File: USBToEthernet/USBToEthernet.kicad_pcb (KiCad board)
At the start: 2 copper layers, 61.3 x 30 mm, 54 parts, among them J1 0480372200, J2 L836-1J1T-43, SW1 SW_Push, U1 LAN7500-ABJZ, U2 NCP1117-3.3_SOT223, U3 93LCxxAxxOT, U4 USBLC6-2SC6, U6 AMS1117-1.2, Y1 25Mhz

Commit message: Reroute again
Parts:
- C1, C10, C11, C12, C13, C14, C15, C16, C17, C18, C19, C2, C20, C21, C26, C27, C3, C4, C5, C6, C7, C8, C9: footprint Capacitor_SMD:C_0603_1608Metric -> Capacitor_SMD:C_0402_1005Metric
- C22, C23, C24, C25: footprint Capacitor_SMD:C_0603_1608Metric -> Capacitor_SMD:C_0402_1005Metric; moved to F.Cu
- FB1, FB2, FB4: footprint Inductor_SMD:L_0603_1608Metric -> Inductor_SMD:L_0402_1005Metric
- FB3, FB5: footprint Inductor_SMD:L_0603_1608Metric -> Inductor_SMD:L_0402_1005Metric; moved to F.Cu
- R1, R10, R11, R12, R13, R2, R3, R4, R5, R6, R7, R8, R9: footprint Resistor_SMD:R_0603_1608Metric -> Resistor_SMD:R_0402_1005Metric
- moved FB1 19.0 mm to (79.3, 88.0)
- moved C6 18.7 mm to (84.9, 96.2), turned to -90 degrees
- moved C10 18.2 mm to (73.4, 93.5), turned to 180 degrees
- moved FB5 17.4 mm to (81.4, 81.3), turned to -90 degrees
- moved C13 17.3 mm to (72.0, 87.8)
- moved R3 17.1 mm to (100.4, 77.3)
- moved C11 17.1 mm to (76.7, 93.7), turned to 180 degrees
- moved C16 16.3 mm to (79.4, 89.1), turned to 180 degrees
- moved C25 16.2 mm to (80.9, 82.8)
- moved C17 15.8 mm to (79.3, 87.0), turned to 180 degrees
- moved C12 15.7 mm to (70.5, 88.2), turned to 180 degrees
- moved FB4 14.9 mm to (82.5, 81.4)
- moved J2 14.1 mm to (96.5, 88.7)
- moved C5 13.9 mm to (84.8, 94.2), turned to 90 degrees
- moved R4 13.8 mm to (102.3, 100.2)
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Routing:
- net GND: track 83.6 -> 30.5 mm, vias 42 -> 43
- net +1V2: track 134.6 -> 86.7 mm, vias 6 -> 9
- net /TR0: track 72.0 -> 46.3 mm, vias 6 -> 8
- net +3V3: track 176.4 -> 160.0 mm, vias 13 -> 11
- net /VBUS: track 27.0 -> 20.4 mm, vias 2 -> 0
- net /RESET: track 22.3 -> 16.6 mm, vias 2 -> 0
- net /VDD12A: track 23.3 -> 17.6 mm
- net /LED2: track 37.3 -> 32.1 mm, vias 2 -> 3
- net /EECLK: track 6.65 -> 1.83 mm
- net /LED1: track 43.2 -> 38.4 mm, vias 3 -> 1
- net /EECS: track 9.01 -> 4.29 mm, vias 0 -> 2
- net /TR2+: track 15.0 -> 10.9 mm
- net /TR3+: track 12.3 -> 8.24 mm
- net /TR3-: track 12.3 -> 8.28 mm
- net /TR2-: track 14.8 -> 10.9 mm
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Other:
- board size 61.3 x 30 mm -> 52.4 x 25.3 mm

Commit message: Reroute and other changes
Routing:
- net GND: track 30.5 -> 32.6 mm, vias 43 -> 45
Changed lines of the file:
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@@
 		(allow_soldermask_bridges_in_footprints no)
 		(tenting front back)
-		(grid_origin 58.275 101.7)
+		(grid_origin 54.525 101.675)
 		(pcbplotparams
 			(layerselection 0x00000000_00000000_55555555_5755f5ff)
@@
 	)
 	(via
+		(at 81.925 98.2)
+		(size 0.6)
+		(drill 0.3)
+		(layers "F.Cu" "B.Cu")
+		(net 1)
+	)
+	(via
 		(at 90.95 78.725)
 		(size 0.5)
@@
 	)
 	(via
+		(at 83.4 96.7)
+		(size 0.6)
+		(drill 0.3)
+		(layers "F.Cu" "B.Cu")
+		(free yes)
+		(net 1)
+	)
+	(via
 		(at 77.45 90.45)
 		(size 0.6)
@@
 	)
 	(segment
+		(start 81.925 98.175)
+		(end 81.925 98.2)
+		(width 0.2)
+		(layer "B.Cu")
+		(net 1)
+	)
+	(segment
 		(start 76.2 93.725)
 		(end 79.01 93.725)
@@
 		(width 0.2)
 		(layer "B.Cu")
+		(net 1)
+	)
+	(segment
+		(start 83.4 96.7)
+		(end 81.925 98.175)
+		(width 0.2)
+		(layer "B.Cu")

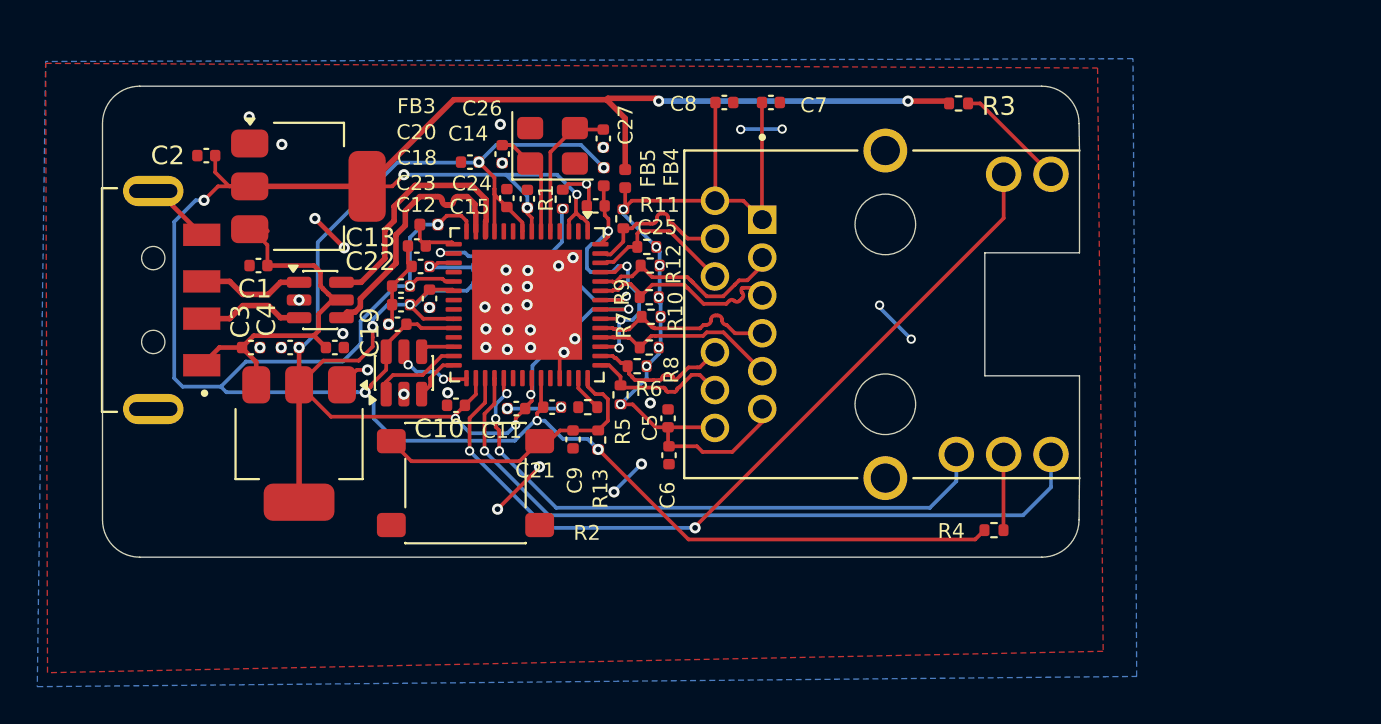
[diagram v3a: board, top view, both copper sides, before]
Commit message: update ibom and production
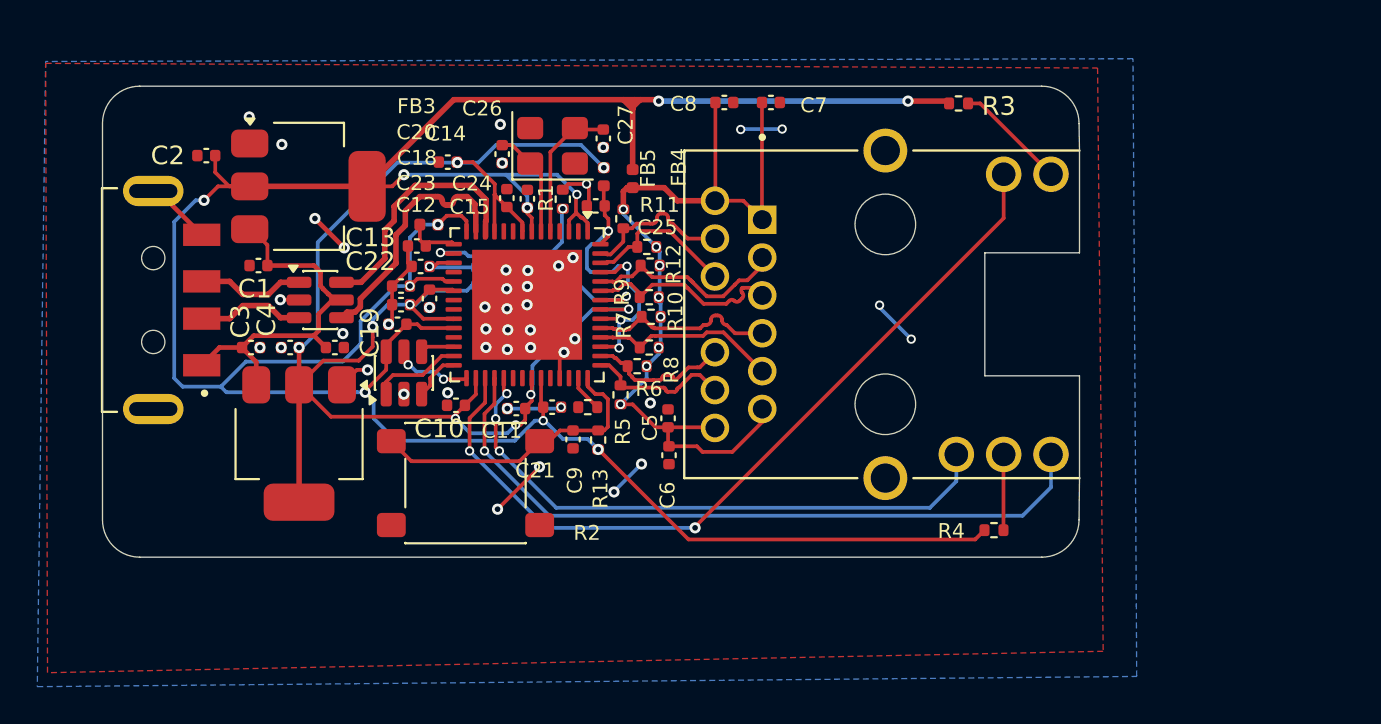
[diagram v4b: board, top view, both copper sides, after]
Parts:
- moved C14 1.19 mm to (73.0, 80.5)
- moved FB4 0.40 mm to (82.9, 81.4)
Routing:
- net GND: track 32.6 -> 33.7 mm
- net +1V2: track 86.7 -> 87.6 mm
- net +3V3: track 160.0 -> 160.8 mm
- added copper zone on In1.Cu, net GND
- added copper zone on In2.Cu, net GND
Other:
- copper layers 2 -> 4
